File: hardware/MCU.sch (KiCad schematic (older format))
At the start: 23 parts, among them J4 Conn_01x03_Male, J5 Conn_02x05_Odd_Even, SW1 SW_Push, U2 STM32F072C8Tx, Y1 Crystal

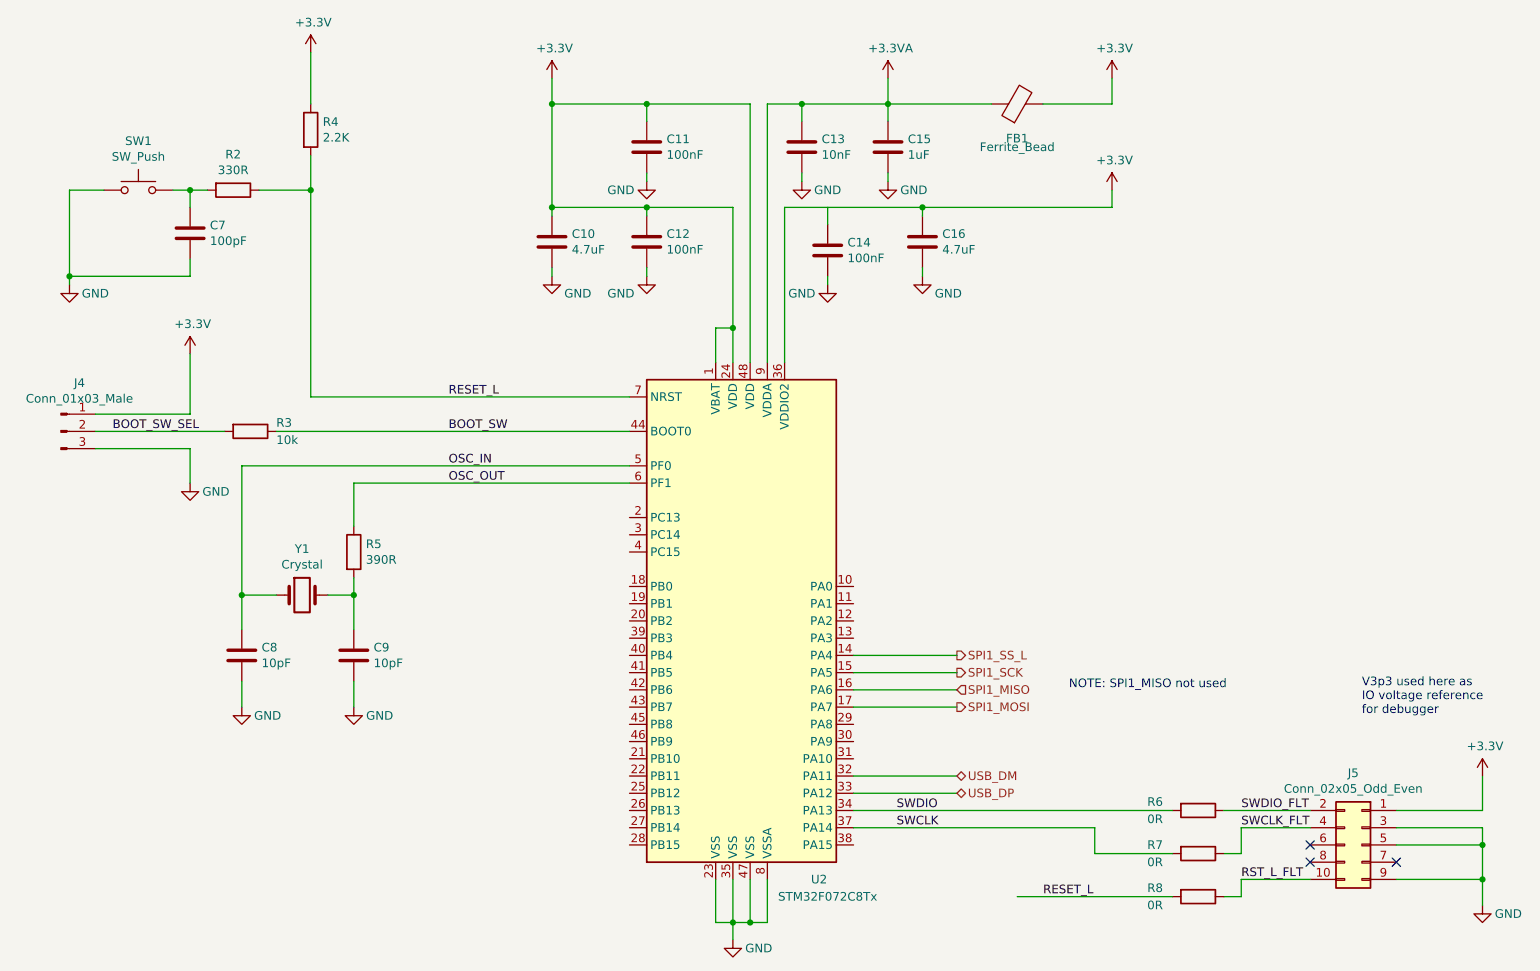
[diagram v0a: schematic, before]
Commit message: Moved all Kicad stuff to /hardware/ directory
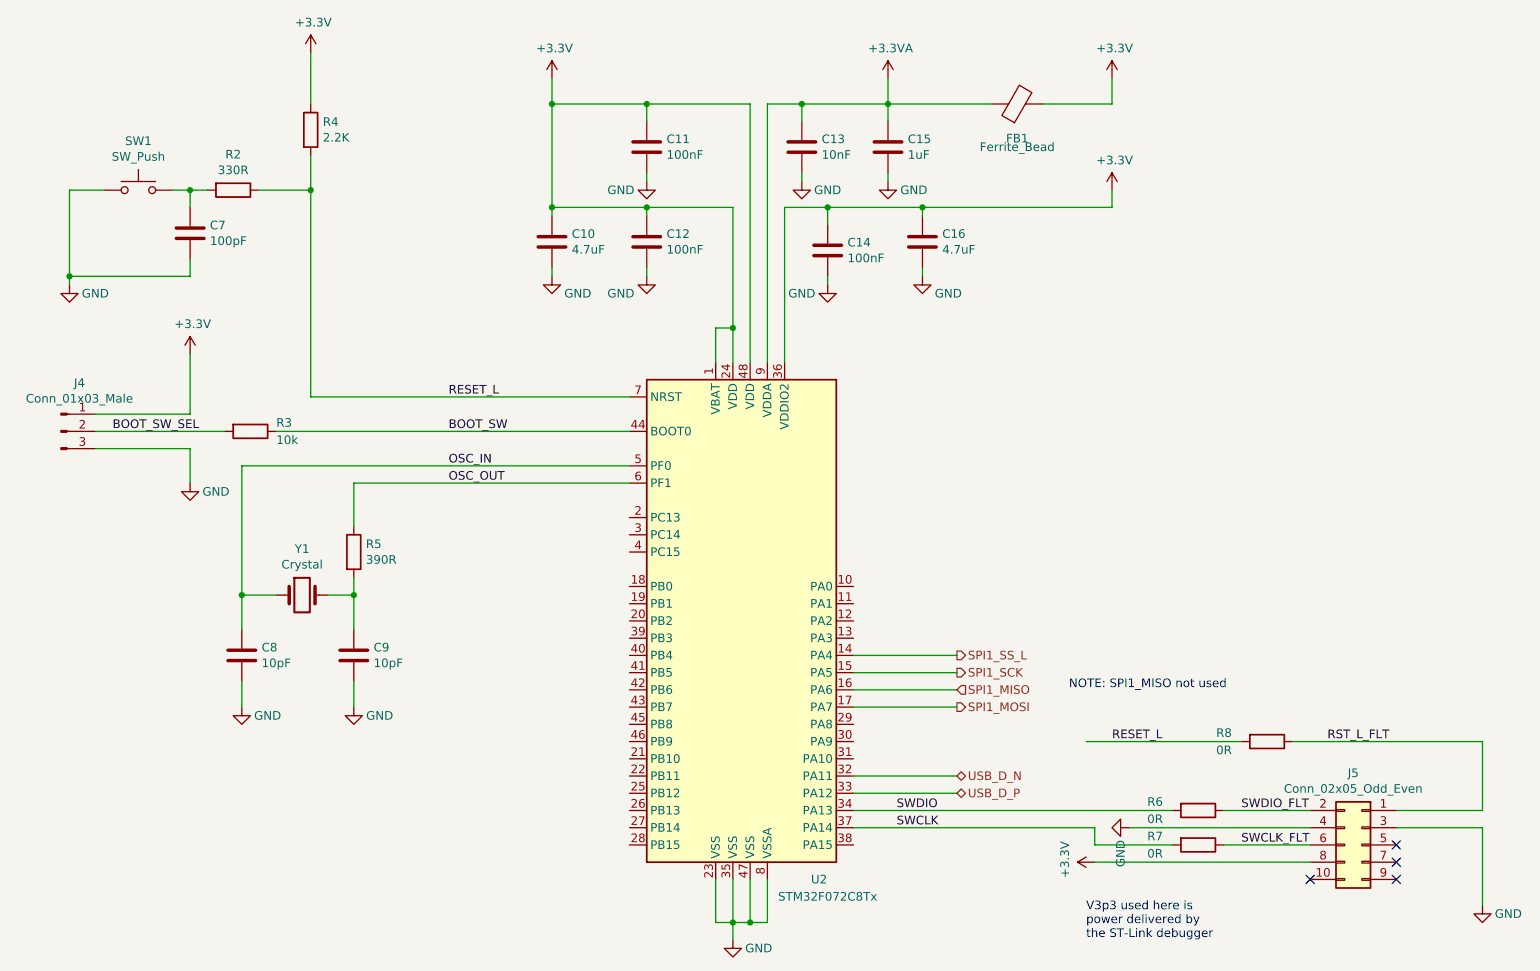
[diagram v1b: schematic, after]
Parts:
- J5: footprint Connector_PinHeader_1.27mm:PinHeader_2x05_P1.27mm_Vertical_SMD -> Connector_PinHeader_2.54mm:PinHeader_2x05_P2.54mm_Vertical
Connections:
- net +3V3: now also C14.1, J5.8 (Pin_8); no longer J5.1 (Pin_1)
- net GND: now also J5.4 (Pin_4); no longer J5.5 (Pin_5), J5.9 (Pin_9)
- net RST_L_FLT: now also J5.1 (Pin_1); no longer J5.10 (Pin_10)
- net SWCLK_FLT: now also J5.6 (Pin_6); no longer J5.4 (Pin_4)
- net USB_DM renamed USB_D_N
- net USB_DP renamed USB_D_P
- no-connect marks 3 -> 4
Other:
- note added: "V3p3 used here is \npower delivered by \nthe ST-Link debugger"
- note removed: "V3p3 used here as \nIO voltage reference \nfor debugger\n"
- moved on the sheet: R7, R8
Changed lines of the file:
@@
 	7500 2050 7500 2000
 Wire Wire Line
-	7500 2000 6700 2000
+	7500 2000 6950 2000
 $Comp
 L power:GND #PWR?
@@
 Connection ~ 6500 6150
 Text HLabel 7700 5300 2    50   BiDi ~ 0
-USB_DM
+USB_D_N
 Text HLabel 7700 5400 2    50   BiDi ~ 0
-USB_DP
+USB_D_P
 Wire Wire Line
 	7700 5400 7100 5400
@@
 F 0 "J5" H 10100 6117 50  0000 C CNN
 F 1 "Conn_02x05_Odd_Even" H 10100 6026 50  0000 C CNN
-F 2 "Connector_PinHeader_1.27mm:PinHeader_2x05_P1.27mm_Vertical_SMD" H 10050 5700 50  0001 C CNN
+F 2 "Connector_PinHeader_2.54mm:PinHeader_2x05_P2.54mm_Vertical" H 10050 5700 50  0001 C CNN
 F 3 "~" H 10050 5700 50  0001 C CNN
 	1    10050 5700
@@
 L Device:R R7
 U 1 1 5E3B73AF
-P 9100 5750
-F 0 "R7" V 9050 5500 50  0000 C CNN
-F 1 "0R" V 9150 5500 50  0000 C CNN
-F 2 "Resistor_SMD:R_0402_1005Metric" V 9030 5750 50  0001 C CNN
-F 3 "~" H 9100 5750 50  0001 C CNN
-	1    9100 5750
+P 9100 5700
+F 0 "R7" V 9050 5450 50  0000 C CNN
+F 1 "0R" V 9150 5450 50  0000 C CNN
+F 2 "Resistor_SMD:R_0402_1005Metric" V 9030 5700 50  0001 C CNN
+F 3 "~" H 9100 5700 50  0001 C CNN
+	1    9100 5700
 	0    1    1    0
 $EndComp
@@
 	7100 5500 8950 5500
 Wire Wire Line
-	8500 5600 8500 5750
-Wire Wire Line
-	8500 5750 8950 5750
-Wire Wire Line
 	7100 5600 8500 5600
-Wire Wire Line
-	9250 5750 9350 5750
-Wire Wire Line
-	9350 5750 9350 5600
-Wire Wire Line
-	9350 5600 9750 5600
 Wire Wire Line
 	9250 5500 9750 5500
 Text Label 9350 5500 0    50   ~ 0
 SWDIO_FLT
-Text Label 9350 5600 0    50   ~ 0
+Text Label 9350 5700 0    50   ~ 0
 SWCLK_FLT
 $Comp
 L power:+3.3V #PWR?
 U 1 1 5E3C1C32
-P 10750 5300
+P 8500 5800
 AR Path="/5E3C1C32" Ref="#PWR?"  Part="1"
 AR Path="/5E381CE2/5E3C1C32" Ref="#PWR032"  Part="1"
-F 0 "#PWR032" H 10750 5150 50  0001 C CNN
-F 1 "+3.3V" H 10765 5473 50  0000 C CNN
-F 2 "" H 10750 5300 50  0001 C CNN
-F 3 "" H 10750 5300 50  0001 C CNN
-	1    10750 5300
-	1    0    0    -1
+F 0 "#PWR032" H 8500 5650 50  0001 C CNN
+F 1 "+3.3V" H 8515 5973 50  0000 C CNN
+F 2 "" H 8500 5800 50  0001 C CNN
+F 3 "" H 8500 5800 50  0001 C CNN
+	1    8500 5800
+	0    -1   -1   0
 $EndComp
 Wire Wire Line
 	10250 5500 10750 5500
 Wire Wire Line
-	10750 5500 10750 5300
-Wire Wire Line
 	10250 5600 10750 5600
-Wire Wire Line
-	10750 5600 10750 5700
-Wire Wire Line
-	10750 5700 10250 5700
-Wire Wire Line
-	10250 5900 10750 5900
-Wire Wire Line
-	10750 5900 10750 5700
-Connection ~ 10750 5700
 $Comp
 L power:GND #PWR?
@@
 	1    0    0    -1
 $EndComp
-Wire Wire Line
-	10750 6050 10750 5900
-Connection ~ 10750 5900
 $Comp
 L Device:R R8
 U 1 1 5E3CD25E
-P 9100 6000
-F 0 "R8" V 9050 5750 50  0000 C CNN
-F 1 "0R" V 9150 5750 50  0000 C CNN
-F 2 "Resistor_SMD:R_0402_1005Metric" V 9030 6000 50  0001 C CNN
-F 3 "~" H 9100 6000 50  0001 C CNN
-	1    9100 6000
+P 9500 5100
+F 0 "R8" V 9450 4850 50  0000 C CNN
+F 1 "0R" V 9550 4850 50  0000 C CNN
+F 2 "Resistor_SMD:R_0402_1005Metric" V 9430 5100 50  0001 C CNN
+F 3 "~" H 9500 5100 50  0001 C CNN
+	1    9500 5100
 	0    1    1    0
 $EndComp
-Wire Wire Line
-	9250 6000 9350 6000
-Wire Wire Line
-	9350 6000 9350 5900
-Wire Wire Line
-	9350 5900 9750 5900
-Text Label 9350 5900 0    50   ~ 0
+Text Label 9850 5100 0    50   ~ 0
 RST_L_FLT
 NoConn ~ 10250 5800
-NoConn ~ 9750 5800
-NoConn ~ 9750 5700
-Wire Wire Line
-	8950 6000 8050 6000
-Text Label 8200 6000 0    50   ~ 0
+Wire Wire Line
+	9350 5100 8450 5100
+Text Label 8600 5100 0    50   ~ 0
 RESET_L
 Wire Wire Line
@@
 Wire Wire Line
 	6400 2700 6400 2900
-Text Notes 10050 4950 0    50   ~ 0
-V3p3 used here as \nIO voltage reference \nfor debugger\n
+Text Notes 8450 6250 0    50   ~ 0
+V3p3 used here is \npower delivered by \nthe ST-Link debugger
 $Comp
 L Device:C C?
@@
 	1    0    0    -1
 $EndComp
+Connection ~ 6950 2000
+Wire Wire Line
+	6950 2000 6700 2000
+Wire Wire Line
+	9250 5700 9750 5700
+Wire Wire Line
+	8950 5700 8500 5700
+Wire Wire Line
+	8500 5700 8500 5600
+$Comp
+L power:GND #PWR?
+U 1 1 5E44CDDB
+P 8700 5600
+AR Path="/5E44CDDB" Ref="#PWR?"  Part="1"
+AR Path="/5E381CE2/5E44CDDB" Ref="#PWR0101"  Part="1"
+F 0 "#PWR0101" H 8700 5350 50  0001 C CNN
+F 1 "GND" H 8850 5550 50  0000 C CNN
+F 2 "" H 8700 5600 50  0001 C CNN
+F 3 "" H 8700 5600 50  0001 C CNN
+	1    8700 5600
+	0    1    1    0
+$EndComp
+Wire Wire Line
+	8700 5600 9750 5600
+Wire Wire Line
+	8500 5800 9750 5800
+Wire Wire Line
+	10750 5100 10750 5500
+Wire Wire Line
+	9650 5100 10750 5100
+Wire Wire Line
+	10750 5600 10750 6050
+NoConn ~ 10250 5900
+NoConn ~ 10250 5700
+NoConn ~ 9750 5900
 $EndSCHEMATC
